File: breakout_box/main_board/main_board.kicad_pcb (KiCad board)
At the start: 2 copper layers, 56 x 120 mm, 39 parts, among them CN1 19PIN_LEMO, Q1 DMP3099L, Q2 MJD122

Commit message: Update schematics
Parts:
- C1, C2, C3, C4: footprint main_board:140CLH-1010 -> Capacitor_SMD:CP_Elec_10x10
- turned C1 to 0 degrees
- turned C2 to 0 degrees
- turned C3 to 0 degrees
- turned C4 to 0 degrees
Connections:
- Q2 pad 1: Net-(C3-Pad+) -> Net-(Q2-Pad1)
- R1 pad 1: Net-(C2-Pad+) -> Net-(R1-Pad1)
- R2 pad 1: Net-(C3-Pad+) -> Net-(Q2-Pad1)
- R2 pad 2: Net-(C2-Pad+) -> Net-(R1-Pad1)
- R3 pad 2: Net-(C3-Pad+) -> Net-(Q2-Pad1)
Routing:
- net Net-(R1-Pad1): track 0.00 -> 41.0 mm
- net Net-(C2-Pad+): track 41.0 -> 0.00 mm
- net Net-(Q2-Pad1): track 0.00 -> 17.3 mm
- net Net-(C3-Pad+): track 17.3 -> 0.00 mm

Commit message: Bump version to 2.6
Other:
- board text added: "Main Board Nexus v2.6"
- board text removed: "Main Board Nexus v2.51"

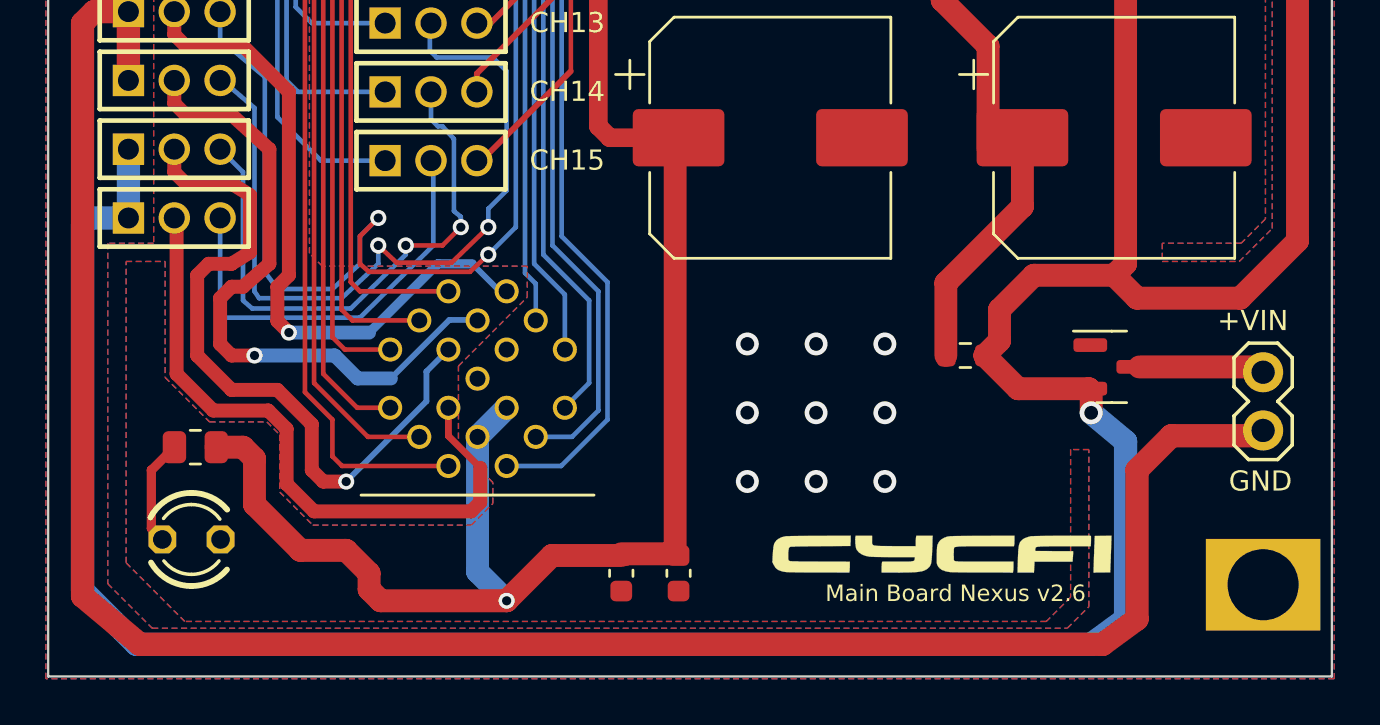
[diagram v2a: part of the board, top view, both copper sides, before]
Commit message: Upgrade to v2.6 - Added short circuit protection - Added soft power switch - Various schematics and PCB layout updates
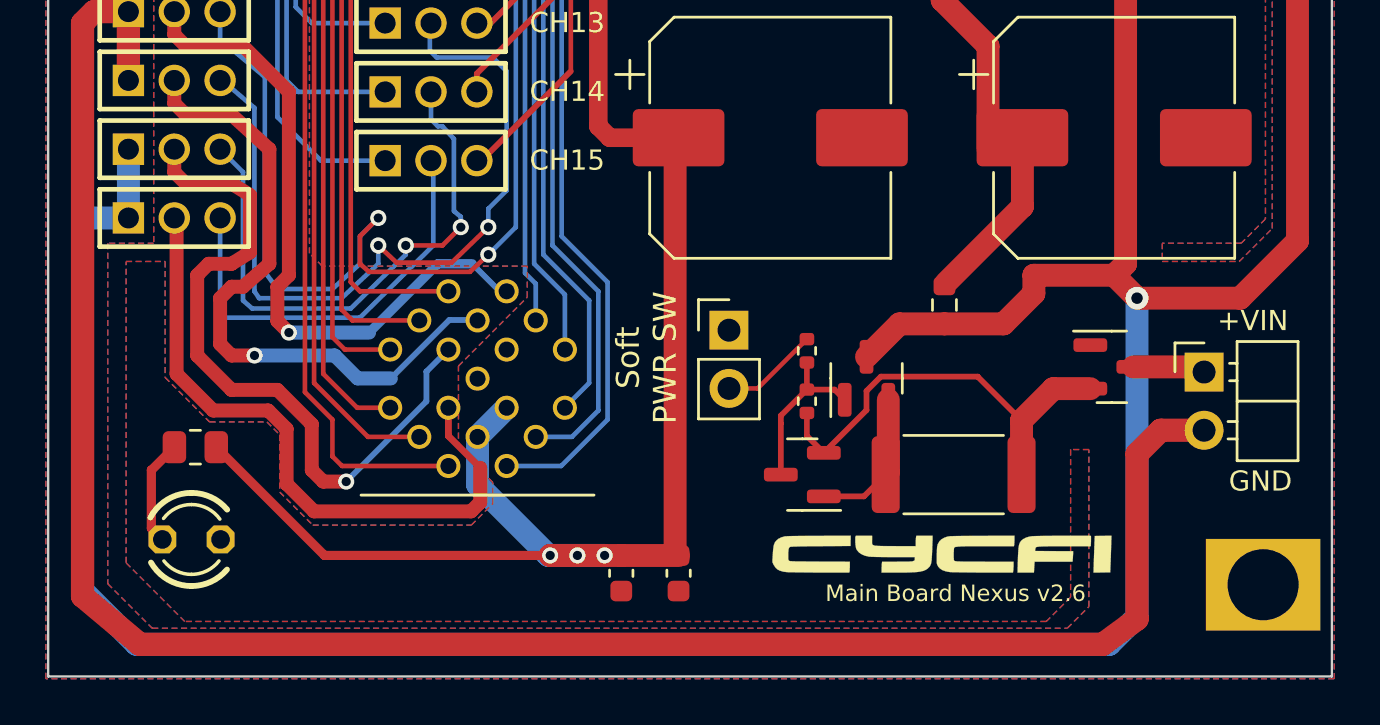
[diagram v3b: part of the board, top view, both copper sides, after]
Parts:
- added H5: MA02-1, Connector_PinHeader_2.54mm:PinHeader_1x02_P2.54mm_Vertical, F.Cu at (150.2, 149.9)
- added Q3: MMBT5401, Package_TO_SOT_SMD:SOT-23, F.Cu at (153.4, 156.2)
- added Q4: DMP3099L, Package_TO_SOT_SMD:SOT-23, F.Cu at (156.2, 152.0)
- added R5: 100K, Resistor_SMD:R_0402_1005Metric, F.Cu at (153.6, 153.0)
- added R6: 10K, Resistor_SMD:R_0402_1005Metric, F.Cu at (153.6, 150.8)
- added R7: 0.36R 2 Watts, Resistor_SMD:R_2512_6332Metric, F.Cu at (160.0, 156.2)
- H6: footprint main_board:MA02-1 -> Connector_PinHeader_2.54mm:PinHeader_1x02_P2.54mm_Horizontal
- moved H6 2.88 mm to (170.9, 151.7), turned to 0 degrees
- moved R1 2.38 mm to (159.6, 148.8), turned to -90 degrees
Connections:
- H6 pad 1: GND -> Net-(Q1-Pad3)
- H6 pad 2: Net-(H6-Pad2) -> GND
- Q1 pad 2: V_AUX -> Net-(Q1-Pad2)
- Q1 pad 3: Net-(H6-Pad2) -> Net-(Q1-Pad3)
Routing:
- net Net-(Q1-Pad2): track 0.00 -> 19.3 mm
- net Net-(Q3-Pad3): track 0.00 -> 7.20 mm
- net Net-(Q3-Pad1): track 0.00 -> 6.40 mm
- net Net-(H6-Pad2): track 5.50 -> 0.00 mm
- net Net-(H5-Pad2): track 0.00 -> 4.29 mm
- net V_AUX: track 194.9 -> 198.4 mm
- net Net-(Q1-Pad3): track 0.00 -> 3.18 mm
- net Net-(C2-Pad1): track 41.0 -> 37.9 mm
- net V_OUT: track 166.0 -> 164.1 mm, vias 1 -> 3
- net GND: track 89.7 -> 87.9 mm, vias 76 -> 67
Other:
- board text added: "Soft PWR SW"

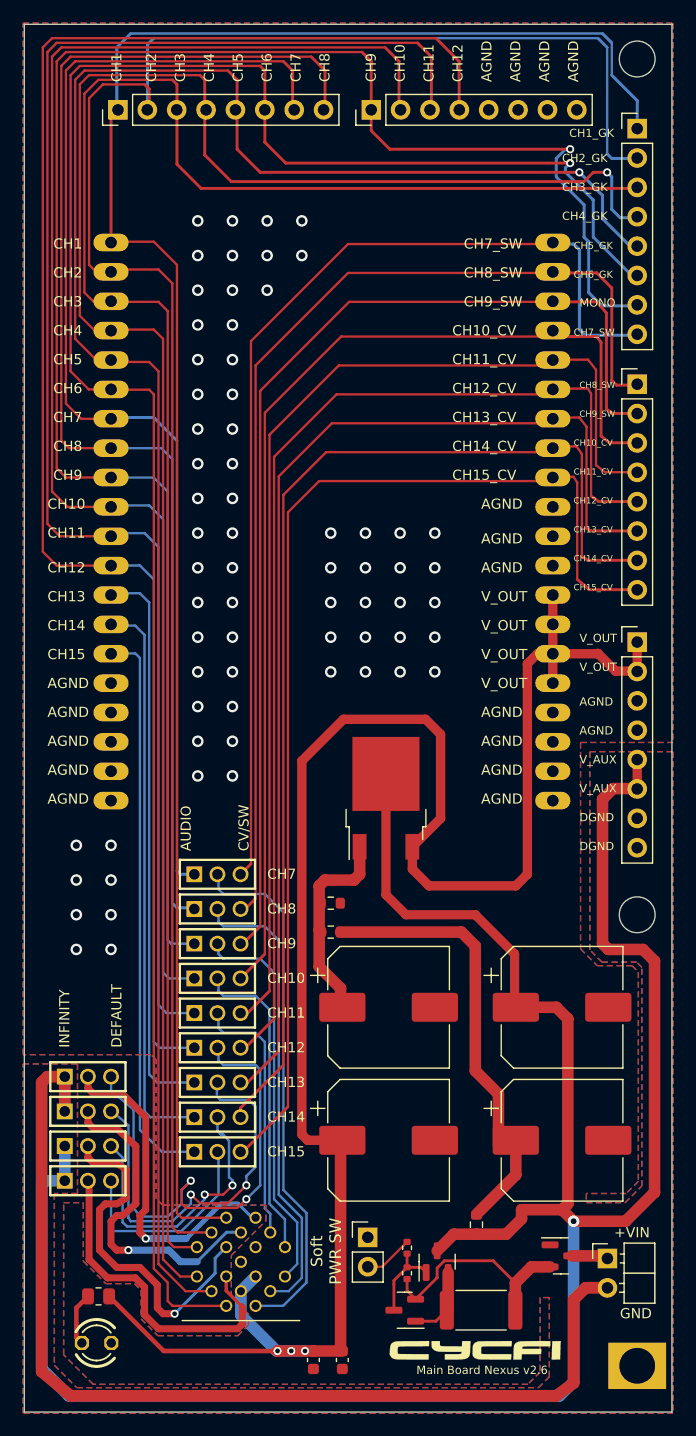
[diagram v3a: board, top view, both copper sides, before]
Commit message: two 1W resistors instead of one 2W resistor
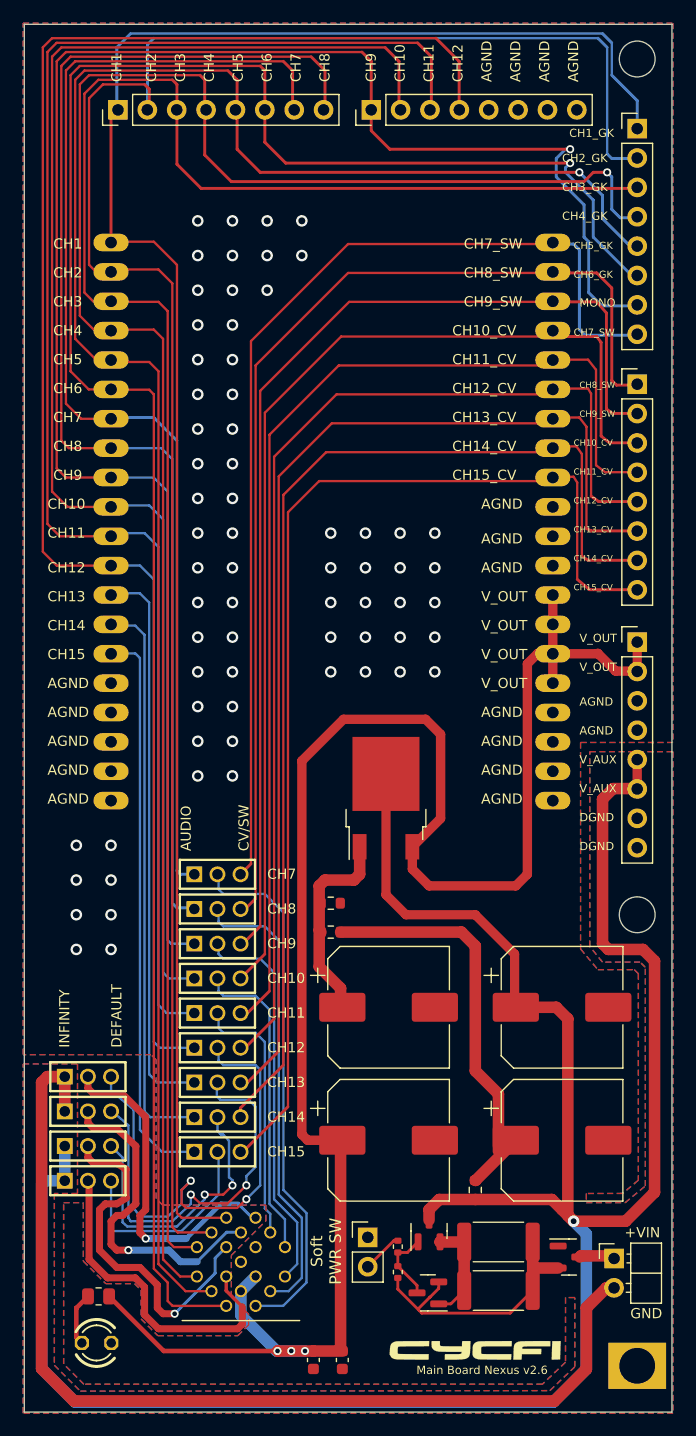
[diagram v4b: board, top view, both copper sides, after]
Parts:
- added R8: 0.75R 1 Watt, Resistor_SMD:R_2512_6332Metric, F.Cu at (161.5, 154.5)
- R7: value 0.36R 2 Watts -> 0.75R 1 Watt
- moved R7 6.09 mm to (161.5, 150.3)
- moved R1 3.00 mm to (159.5, 145.8)
- moved Q4 2.74 mm to (155.5, 149.3)
- moved Q3 2.50 mm to (155.4, 154.7)
- moved R6 0.81 mm to (152.8, 150.7)
- moved R5 0.81 mm to (152.8, 152.9)
- moved Q1 0.71 mm to (167.6, 151.6)
- moved H6 0.57 mm to (171.5, 151.7)
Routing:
- net Net-(Q1-Pad2): track 19.3 -> 24.0 mm
- net V_AUX: track 198.4 -> 201.1 mm
- net Net-(C2-Pad1): track 37.9 -> 35.2 mm
- net Net-(Q3-Pad1): track 6.40 -> 8.97 mm
- net Net-(Q3-Pad3): track 7.20 -> 6.31 mm
- net Net-(H5-Pad2): track 4.29 -> 3.53 mm

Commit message: some tweaks
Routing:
- net V_AUX: track 201.1 -> 204.2 mm, vias 1 -> 3
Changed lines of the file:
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@@
   (segment (start 171.4111 111.0936) (end 170.5011 112.0036) (width 1) (layer "F.Cu") (net 18))
   (segment (start 167.5011 131.0036) (end 167.5011 148.0036) (width 1) (layer "F.Cu") (net 18))
+  (segment (start 169.05 149.6) (end 169.05 149.5525) (width 1) (layer "F.Cu") (net 18))
   (segment (start 155.5 147.5) (end 156.375 146.625) (width 1) (layer "F.Cu") (net 18))
   (segment (start 153.5011 122.0036) (end 151.775 120.2775) (width 0.8) (layer "F.Cu") (net 18))
@@
   (segment (start 175.0011 126.0036) (end 175.0011 146.0036) (width 1) (layer "F.Cu") (net 18))
   (segment (start 170.5011 112.0036) (end 170.5011 124.5036) (width 1) (layer "F.Cu") (net 18))
+  (segment (start 169.05 149.5525) (end 168.0011 148.5036) (width 1) (layer "F.Cu") (net 18))
   (segment (start 167.5011 148.0036) (end 168.0011 148.5036) (width 1) (layer "F.Cu") (net 18))
   (segment (start 170.5011 124.5036) (end 171.0011 125.0036) (width 1) (layer "F.Cu") (net 18))
   (segment (start 156.375 146.625) (end 159.5 146.625) (width 1) (layer "F.Cu") (net 18))
+  (via (at 166.95 147.4) (size 1) (drill 0.5) (layers "F.Cu" "B.Cu") (net 18))
   (via (at 168.0011 148.5036) (size 1) (drill 0.5) (layers "F.Cu" "B.Cu") (net 18))
+  (via (at 169.05 149.6) (size 1) (drill 0.5) (layers "F.Cu" "B.Cu") (net 18))
   (segment (start 124.0011 145.0036) (end 122.2511 145.0036) (width 1) (layer "B.Cu") (net 18))
   (segment (start 124.8975 164.15) (end 166.25 164.15) (width 1) (layer "B.Cu") (net 18))
+  (segment (start 168.0011 148.4511) (end 166.95 147.4) (width 1) (layer "B.Cu") (net 18))
   (segment (start 122.0011 161.2536) (end 124.8975 164.15) (width 1) (layer "B.Cu") (net 18))
   (segment (start 169.1 161.3) (end 169.1 149.6025) (width 1) (layer "B.Cu") (net 18))
@@
   (segment (start 169.1 149.6025) (end 168.0011 148.5036) (width 1) (layer "B.Cu") (net 18))
   (segment (start 124.0011 142.0036) (end 124.0011 145.0036) (width 1) (layer "B.Cu") (net 18))
+  (segment (start 168.0011 148.5036) (end 168.0011 148.4511) (width 1) (layer "B.Cu") (net 18))
   (segment (start 166.25 164.15) (end 169.1 161.3) (width 1) (layer "B.Cu") (net 18))
   (segment (start 140.1011 117.6036) (end 139.2011 118.5036) (width 0.254) (layer "F.Cu") (net 19))
